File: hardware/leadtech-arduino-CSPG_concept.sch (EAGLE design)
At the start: 48 parts, among them IC1 OP-AMP, IC3 4050D, J1 CON_HEADER_1X08-PTH, J2 CON_HEADER_1X04, J3 CON_HEADER_1X03-PTH, J9 CON_HEADER_1X02-PTH, Q1 16Mhz, U1 DS1302, U3 PL2303HX

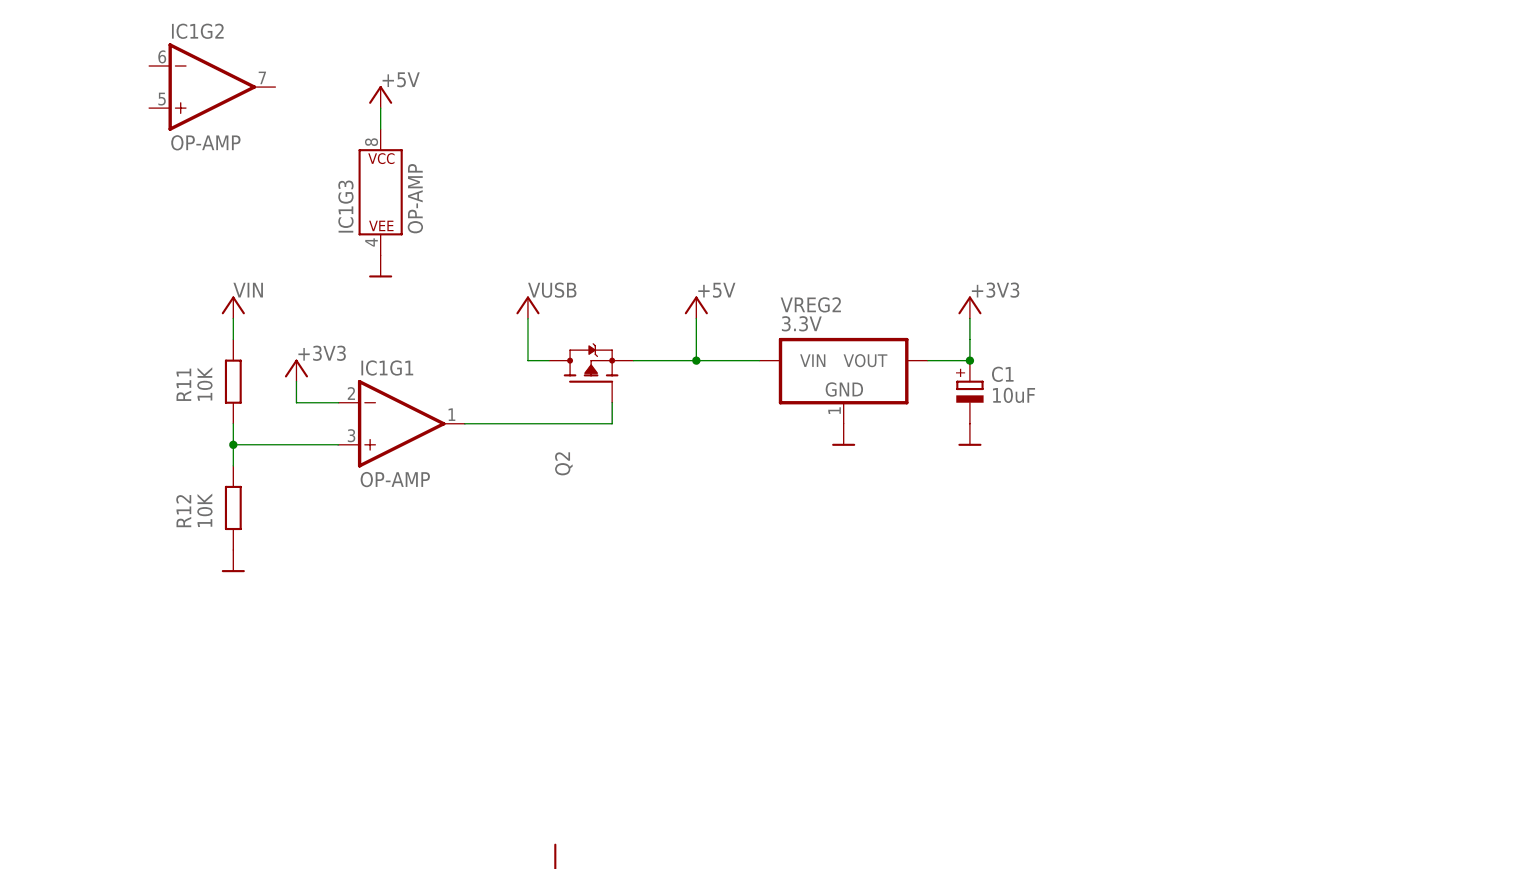
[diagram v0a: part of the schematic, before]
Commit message: add power source manager op-amp wiring
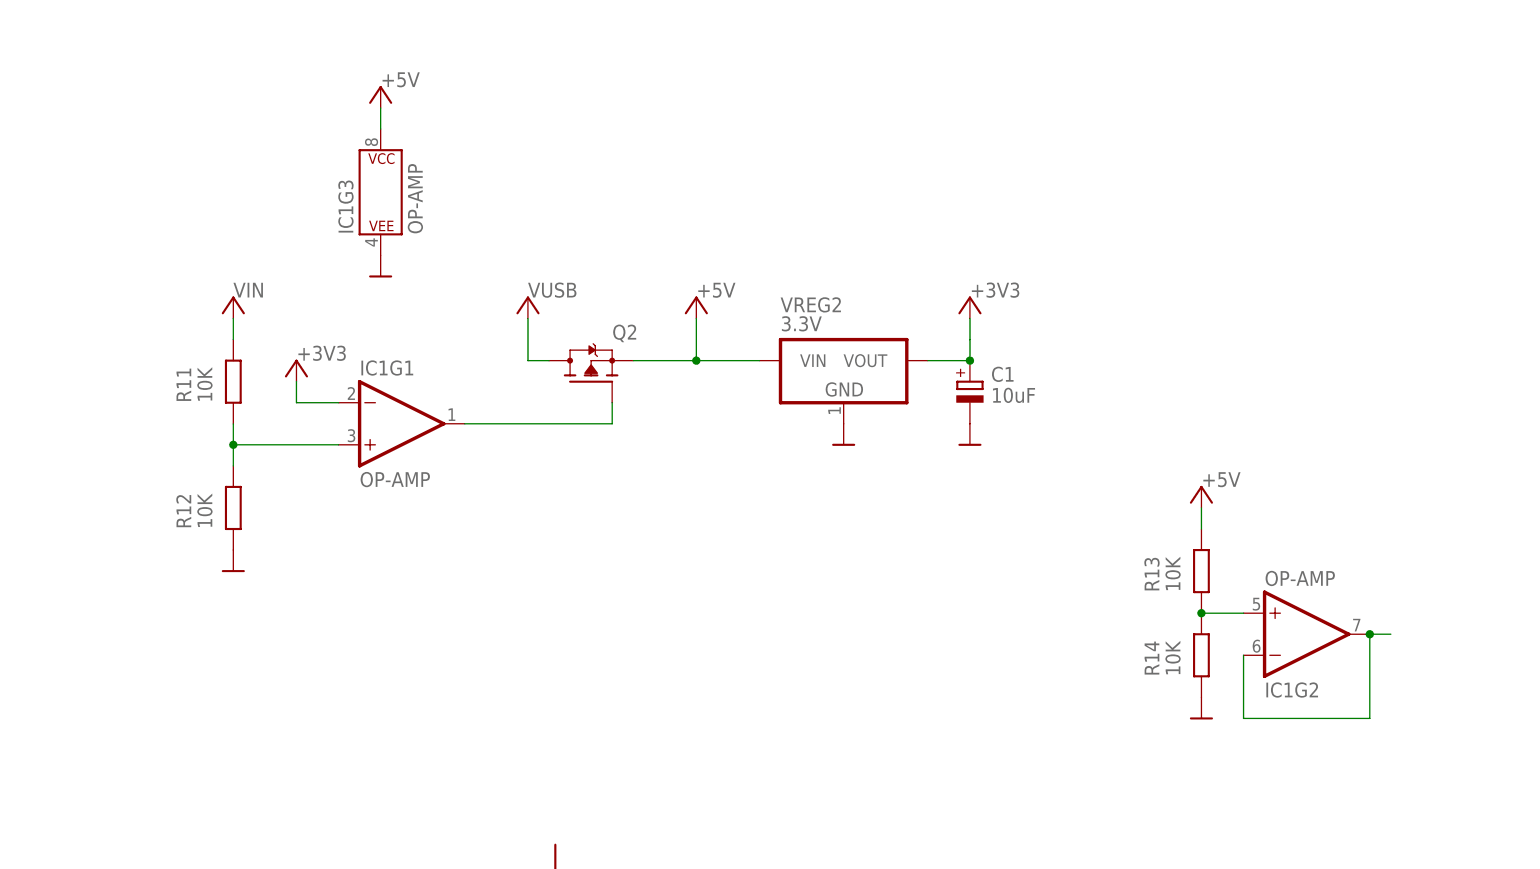
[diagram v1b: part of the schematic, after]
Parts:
- added R13, R14: 10K, dp_devices.v6:RESISTOR-0603
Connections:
- new net N$6: IC1G2.-IN, IC1G2.OUT
- new net N$9: IC1G2.+IN, R13.1, R14.2
- net +5V: now also R13.2
- net GND: now also R14.1
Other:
- note added: "If VIN is present, VUSB is cut and system is powered by VIN, otherwise via VUSB"
- note added: "Unused"
- moved on the sheet: IC1G2
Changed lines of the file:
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@@
 <part name="+5V21" library="dp_devices.v6" deviceset="SUPPLY_+5V" device=""/>
 <part name="+5V22" library="dp_devices.v6" deviceset="SUPPLY_+5V" device=""/>
+<part name="R13" library="dp_devices.v6" deviceset="RESISTOR" device="-0603" value="10K"/>
+<part name="R14" library="dp_devices.v6" deviceset="RESISTOR" device="-0603" value="10K"/>
+<part name="GND6" library="dp_devices.v6" deviceset="SUPPLY_GND" device=""/>
+<part name="+5V23" library="dp_devices.v6" deviceset="SUPPLY_+5V" device=""/>
 </parts>
 <sheets>
@@
 <text x="359.664" y="116.586" size="1.778" layer="98" align="center">6</text>
 <text x="350.52" y="91.44" size="1.778" layer="98" align="center">5</text>
+<text x="226.06" y="215.9" size="1.778" layer="98" align="center">If VIN is present, VUSB is cut and
+system is powered by VIN,
+otherwise via VUSB</text>
+<text x="289.56" y="185.42" size="1.778" layer="98" align="center">Unused</text>
 </plain>
 <instances>
@@
 <instance part="Q2" gate="Q" x="208.28" y="231.14" smashed="yes" rot="R90">
 <attribute name="VALUE" x="208.28" y="219.71" size="1.778" layer="96" rot="R90"/>
-<attribute name="NAME" x="205.74" y="219.71" size="1.778" layer="95" rot="R90"/>
+<attribute name="NAME" x="210.82" y="236.22" size="1.778" layer="95"/>
 </instance>
 <instance part="+5V3" gate="SUPPLY" x="200.66" y="238.76" smashed="yes"/>
@@
 <attribute name="VALUE" x="187.96" y="248.92" size="1.778" layer="95" font="vector" rot="R90"/>
 </instance>
-<instance part="IC1" gate="G2" x="162.56" y="266.7" smashed="yes">
-<attribute name="NAME" x="157.48" y="272.542" size="1.778" layer="95" font="vector"/>
-<attribute name="VALUE" x="157.48" y="259.08" size="1.778" layer="95" font="vector"/>
+<instance part="IC1" gate="G2" x="294.64" y="200.66" smashed="yes" rot="MR180">
+<attribute name="NAME" x="289.56" y="194.818" size="1.778" layer="95" font="vector" rot="MR180"/>
+<attribute name="VALUE" x="289.56" y="208.28" size="1.778" layer="95" font="vector" rot="MR180"/>
 </instance>
 <instance part="GND3" gate="G$1" x="182.88" y="243.84" smashed="yes"/>
@@
 <instance part="+5V21" gate="SUPPLY" x="48.26" y="162.56" smashed="yes"/>
 <instance part="+5V22" gate="SUPPLY" x="165.1" y="238.76" smashed="yes"/>
+<instance part="R13" gate="R" x="281.94" y="208.28" smashed="yes" rot="R90">
+<attribute name="NAME" x="276.86" y="205.74" size="1.778" layer="95" font="vector" rot="R90"/>
+<attribute name="VALUE" x="279.4" y="205.74" size="1.778" layer="96" font="vector" rot="R90"/>
+</instance>
+<instance part="R14" gate="R" x="281.94" y="198.12" smashed="yes" rot="R90">
+<attribute name="NAME" x="276.86" y="195.58" size="1.778" layer="95" font="vector" rot="R90"/>
+<attribute name="VALUE" x="279.4" y="195.58" size="1.778" layer="96" font="vector" rot="R90"/>
+</instance>
+<instance part="GND6" gate="G$1" x="281.94" y="190.5" smashed="yes"/>
+<instance part="+5V23" gate="SUPPLY" x="281.94" y="215.9" smashed="yes"/>
 </instances>
 <busses>
@@
 <pinref part="R12" gate="R" pin="1"/>
 <pinref part="GND5" gate="G$1" pin="GND"/>
+</segment>
+<segment>
+<pinref part="R14" gate="R" pin="1"/>
+<pinref part="GND6" gate="G$1" pin="GND"/>
 </segment>
 </net>
@@
 <pinref part="+5V18" gate="SUPPLY" pin="+5V"/>
 <label x="220.98" y="241.3" size="1.778" layer="95"/>
+</segment>
+<segment>
+<pinref part="R13" gate="R" pin="2"/>
+<pinref part="+5V23" gate="SUPPLY" pin="+5V"/>
+<wire x1="281.94" y1="215.9" x2="281.94" y2="213.36" width="0.1524" layer="91"/>
+<label x="281.94" y="218.44" size="1.778" layer="95"/>
 </segment>
 </net>
@@
 </segment>
 </net>
+<net name="N$6" class="0">
+<segment>
+<pinref part="IC1" gate="G2" pin="-IN"/>
+<wire x1="287.02" y1="198.12" x2="287.02" y2="190.5" width="0.1524" layer="91"/>
+<pinref part="IC1" gate="G2" pin="OUT"/>
+<wire x1="287.02" y1="190.5" x2="302.26" y2="190.5" width="0.1524" layer="91"/>
+<wire x1="302.26" y1="190.5" x2="302.26" y2="200.66" width="0.1524" layer="91"/>
+<wire x1="302.26" y1="200.66" x2="304.8" y2="200.66" width="0.1524" layer="91"/>
+<junction x="302.26" y="200.66"/>
+</segment>
+</net>
+<net name="N$9" class="0">
+<segment>
+<pinref part="IC1" gate="G2" pin="+IN"/>
+<wire x1="287.02" y1="203.2" x2="281.94" y2="203.2" width="0.1524" layer="91"/>
+<pinref part="R13" gate="R" pin="1"/>
+<pinref part="R14" gate="R" pin="2"/>
+<junction x="281.94" y="203.2"/>
+</segment>
+</net>

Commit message: continue routing board
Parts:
- removed VREG1: 7805, dp_devices.v6:VREG_3PINS-TO-220V
- removed VREG2: 3.3V, dp_devices.v6:VREG_3PINS-SOT-223
- added C16: 0.1uF, rcl:C-EUC0603
- added J4: CON_HEADER_1X02-PTH, dp_devices.v6:CON_HEADER_1X02-PTH
- added U2: VREG-78M05, trosh_devices.eagle.v9:VREG-78M05
- added U4: MP1584EN_MODULE, trosh_devices.eagle.v9:MP1584EN_MODULE
- added U5: VREG-RT9163-3.3V, trosh_devices.eagle.v9:VREG-RT9163
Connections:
- new net N$7: J4.1, U4.VIN+
- net +3V3: now also U5.VOUT; no longer VREG2.VOUT
- net +5V: now also C16.2, U2.VOUT, U5.VIN; no longer VREG1.VOUT, VREG2.VIN
- net GND: now also C16.1, J4.2, U2.GND, U4.VIN-, U4.VOUT-, U5.GND; no longer VREG1.GND, VREG2.GND
- net N$19: now also U4.VOUT+
- net VIN: now also U2.VIN; no longer VREG1.VIN
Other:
- note added: "use BOOMELE(Boom Precision Elec) part no. C27543"
- note removed: "TO DO: place DC-DC power supply"
- moved on the sheet: C14, C8, C9, D1, J9

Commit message: routing
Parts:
- added J5: CON_HEADER_1X02-PTH, dp_devices.v6:CON_HEADER_1X02-PTH
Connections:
- net GND: now also J5.2
- net SW1: now also J5.1
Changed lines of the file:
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@@
 <?xml version="1.0" encoding="utf-8"?>
 <!DOCTYPE eagle SYSTEM "eagle.dtd">
-<eagle version="9.4.2">
+<eagle version="9.1.3">
 <drawing>
 <settings>
@@
 <part name="C16" library="rcl" library_urn="urn:adsk.eagle:library:334" deviceset="C-EU" device="C0603" package3d_urn="urn:adsk.eagle:package:23616/2" value="0.1uF"/>
 <part name="U5" library="trosh_devices.eagle.v9" deviceset="VREG-RT9163" device="" value="VREG-RT9163-3.3V"/>
+<part name="J5" library="dp_devices.v6" deviceset="CON_HEADER_1X02" device="-PTH"/>
+<part name="GND33" library="dp_devices.v6" deviceset="SUPPLY_GND" device=""/>
 </parts>
 <sheets>
@@
 <attribute name="VALUE" x="231.14" y="237.236" size="1.778" layer="96"/>
 </instance>
+<instance part="J5" gate="J" x="284.48" y="106.68" smashed="yes" rot="MR0">
+<attribute name="NAME" x="285.75" y="110.49" size="1.778" layer="95" rot="MR0"/>
+</instance>
+<instance part="GND33" gate="G$1" x="287.02" y="99.06" smashed="yes"/>
 </instances>
 <busses>
@@
 <segment>
 <pinref part="U5" gate="U" pin="GND"/>
-<pinref part="U5" gate="U" pin="GND"/>
 <pinref part="GND1" gate="G$1" pin="GND"/>
 <junction x="238.76" y="226.06"/>
+</segment>
+<segment>
+<pinref part="J5" gate="J" pin="2"/>
+<pinref part="GND33" gate="G$1" pin="GND"/>
+<wire x1="284.48" y1="104.14" x2="287.02" y2="104.14" width="0.1524" layer="91"/>
+<wire x1="287.02" y1="104.14" x2="287.02" y2="101.6" width="0.1524" layer="91"/>
 </segment>
 </net>
@@
 <junction x="322.58" y="93.98"/>
 </segment>
-</net>
+<segment>
+<pinref part="J5" gate="J" pin="1"/>
+<wire x1="284.48" y1="106.68" x2="287.02" y2="106.68" width="0.1524" layer="91"/>
+<label x="287.02" y="106.68" size="1.778" layer="95"/>
+</segment>
+</net>

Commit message: routing
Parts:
- removed C14: 100uF, dp_devices.v6:CAPACITOR_POL-CASE_B
- removed J3: CON_HEADER_1X03-PTH, dp_devices.v6:CON_HEADER_1X03-PTH
- added R15: 100R, rcl:R-EU_R0603
- C1: value 10uF -> 100uF
- U5: value VREG-RT9163-3.3V -> RT9163-3.3V
- renumbered U$1 to U6
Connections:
- removed net N$1: J3.3
- removed net N$2: J3.2
- new net N$20: R15.2, SG1.+
- net +3V3: no longer C14.+
- net GND: no longer C14.-, J3.1
- net PIEZO: now also R15.1; no longer SG1.+
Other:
- note added: "BUTTON"
- note added: "SUPPLY HANDOVER"
- note removed: "TO DO: make CR2032 battery socket make circuit for the control relay build DC-DC for power supply"
- moved on the sheet: C1, C10, C16, C8, C9, D1, G1, IC1G1, IC1G2, IC1G3, J1, J2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

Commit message: 1
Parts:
- removed G1: CR2032H, battery:CR2032H
- added BATT1: CR2032, trosh_devices.eagle.v9:CR2032
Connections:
- net GND: now also BATT1.B-; no longer G1.-
- net N$24: now also BATT1.B+; no longer G1.+
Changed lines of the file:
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@@
 <?xml version="1.0" encoding="utf-8"?>
 <!DOCTYPE eagle SYSTEM "eagle.dtd">
-<eagle version="9.4.2">
+<eagle version="9.1.3">
 <drawing>
 <settings>
@@
 <part name="+5V11" library="dp_devices.v6" deviceset="SUPPLY_+5V" device=""/>
 <part name="GND23" library="dp_devices.v6" deviceset="SUPPLY_GND" device=""/>
-<part name="G1" library="battery" library_urn="urn:adsk.eagle:library:109" deviceset="CR2032H" device="" package3d_urn="urn:adsk.eagle:package:4585/1"/>
 <part name="GND24" library="dp_devices.v6" deviceset="SUPPLY_GND" device=""/>
 <part name="FRAME1" library="frames" library_urn="urn:adsk.eagle:library:229" deviceset="A4L-LOC" device=""/>
@@
 <part name="GND33" library="dp_devices.v6" deviceset="SUPPLY_GND" device=""/>
 <part name="R15" library="rcl" library_urn="urn:adsk.eagle:library:334" deviceset="R-EU_" device="R0603" package3d_urn="urn:adsk.eagle:package:23555/3" value="100R"/>
+<part name="BATT1" library="trosh_devices.eagle.v9" deviceset="CR2032" device=""/>
 </parts>
 <sheets>
@@
 <instance part="+5V11" gate="SUPPLY" x="60.96" y="43.18" smashed="yes" rot="R90"/>
 <instance part="GND23" gate="G$1" x="223.52" y="124.46" smashed="yes"/>
-<instance part="G1" gate="1" x="241.3" y="132.08" smashed="yes" rot="R90">
-<attribute name="NAME" x="243.84" y="129.54" size="1.778" layer="95"/>
-<attribute name="VALUE" x="243.84" y="127" size="1.778" layer="96"/>
-</instance>
 <instance part="GND24" gate="G$1" x="241.3" y="124.46" smashed="yes"/>
 <instance part="FRAME1" gate="G$1" x="0" y="0" smashed="yes">
@@
 <attribute name="VALUE" x="434.34" y="63.5" size="1.778" layer="96"/>
 </instance>
+<instance part="BATT1" gate="BATT" x="241.3" y="132.08" smashed="yes">
+<attribute name="NAME" x="248.92" y="134.62" size="1.778" layer="95" align="bottom-center"/>
+<attribute name="VALUE" x="248.92" y="132.08" size="1.778" layer="96" align="bottom-center"/>
+</instance>
 </instances>
 <busses>
@@
 </segment>
 <segment>
-<pinref part="G1" gate="1" pin="-"/>
 <pinref part="GND24" gate="G$1" pin="GND"/>
+<pinref part="BATT1" gate="BATT" pin="B-"/>
 </segment>
 <segment>
@@
 <segment>
 <pinref part="U1" gate="U" pin="VCC1"/>
-<pinref part="G1" gate="1" pin="+"/>
 <wire x1="238.76" y1="137.16" x2="241.3" y2="137.16" width="0.1524" layer="91"/>
-</segment>
-</net>
+<pinref part="BATT1" gate="BATT" pin="B+"/>
+</segment>
+</net>

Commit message: routing
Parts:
- removed J2: CON_HEADER_1X04, dp_devices.v6:CON_HEADER_1X04
- removed J4: CON_HEADER_1X02-PTH, dp_devices.v6:CON_HEADER_1X02-PTH
- added C14: 0.1uF, rcl:C-EUC0603
- added C17, C18: 10uF, dp_devices.v6:CAPACITOR_POL-CASE_B
- added J3: CON_HX42003_2, trosh_devices.eagle.v9:CON_HX42003_2
- added J6: 2510-4AGW, trosh_devices.eagle.v9:CON_KF2510-4AGW-2
- added MOD1: ESP8266-07, trosh_devices.eagle.v9:ESP8266-07
- added R16, R17, R18, R19, R20: 10K, dp_devices.v6:RESISTOR-0603
- added U7: AZ1117CH2-3.3TRG1, trosh_devices.eagle.v9:VREG-RT9163
- BATT1: value CR2032 -> CR2032-BS-6-1
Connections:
- new net +3V3_ESP: C14.2, C17.+, MOD1.VCC, U7.VOUT
- new net ESP_RXD: IC3F.I, U6.PD3
- new net ESP_TXD: MOD1.TXD, U6.PD2
- new net N$1: MOD1.!RST, R16.1
- new net N$2: MOD1.EN, R17.1
- new net N$25: MOD1.IO15, R18.2
- new net N$26: MOD1.IO2, R19.2
- new net N$27: MOD1.IO0, R20.2
- new net N$28: IC3F.O, MOD1.RXD
- net +3V3: now also R16.2, R17.2, R19.1, R20.1
- net +5V: now also C18.+, J6.4, U7.VIN; no longer J2.1
- net DISPLAY_I2C_CLOCK: now also J6.2; no longer J2.3
- net DISPLAY_I2C_DATA: now also J6.1; no longer J2.4
- net GND: now also C14.1, C17.-, C18.-, J3.2, J6.3, MOD1.GND, R18.1, U7.GND; no longer J2.2, J4.2
- net N$22: now also XTAL1.1; no longer XTAL1.2
- net N$23: now also XTAL1.2; no longer XTAL1.1
- net N$7: now also J3.1; no longer J4.1
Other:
- moved on the sheet: C11, C12, C13, C2, C3, J1, Q1, R1, R10, R2, R5, U6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
